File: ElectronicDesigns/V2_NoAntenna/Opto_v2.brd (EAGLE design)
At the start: 87.5 x 48 mm, 5 parts, among them U1 TLV1117-18IDCYG3

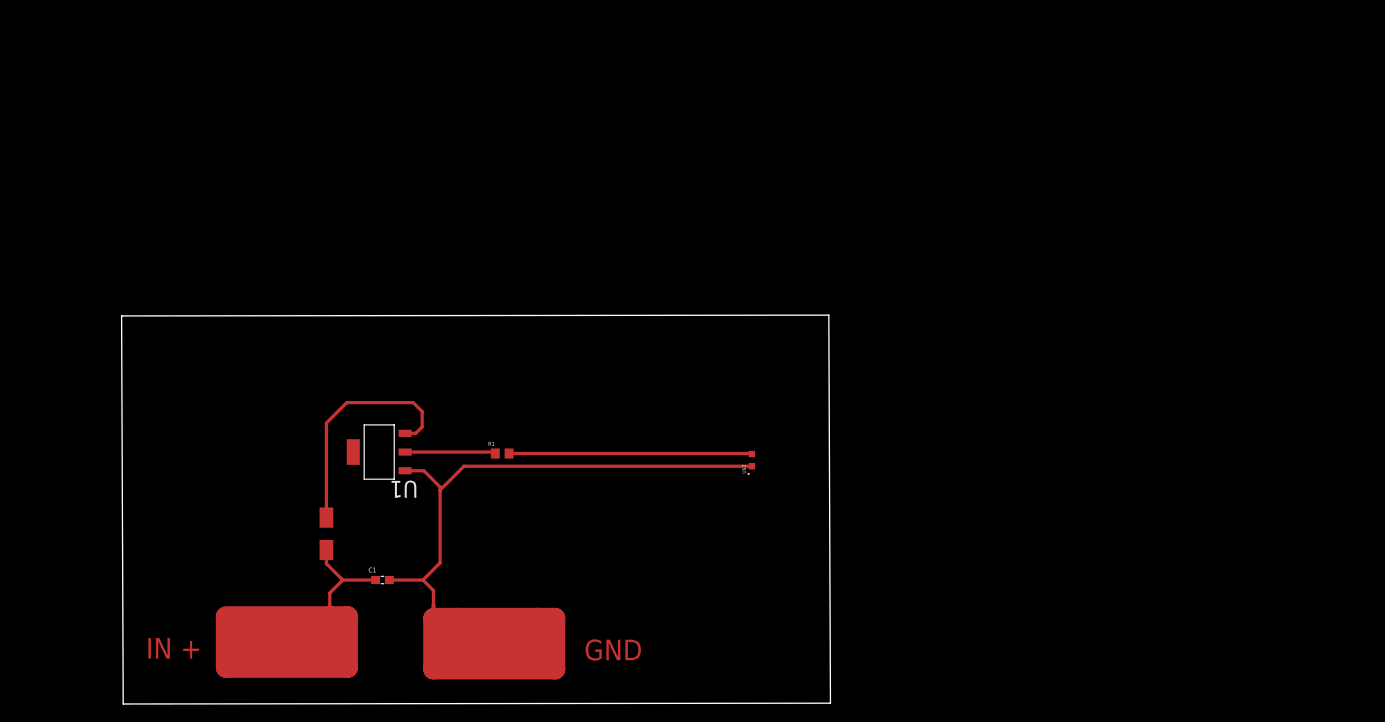
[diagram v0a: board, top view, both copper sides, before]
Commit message: antenna-circuit assembled
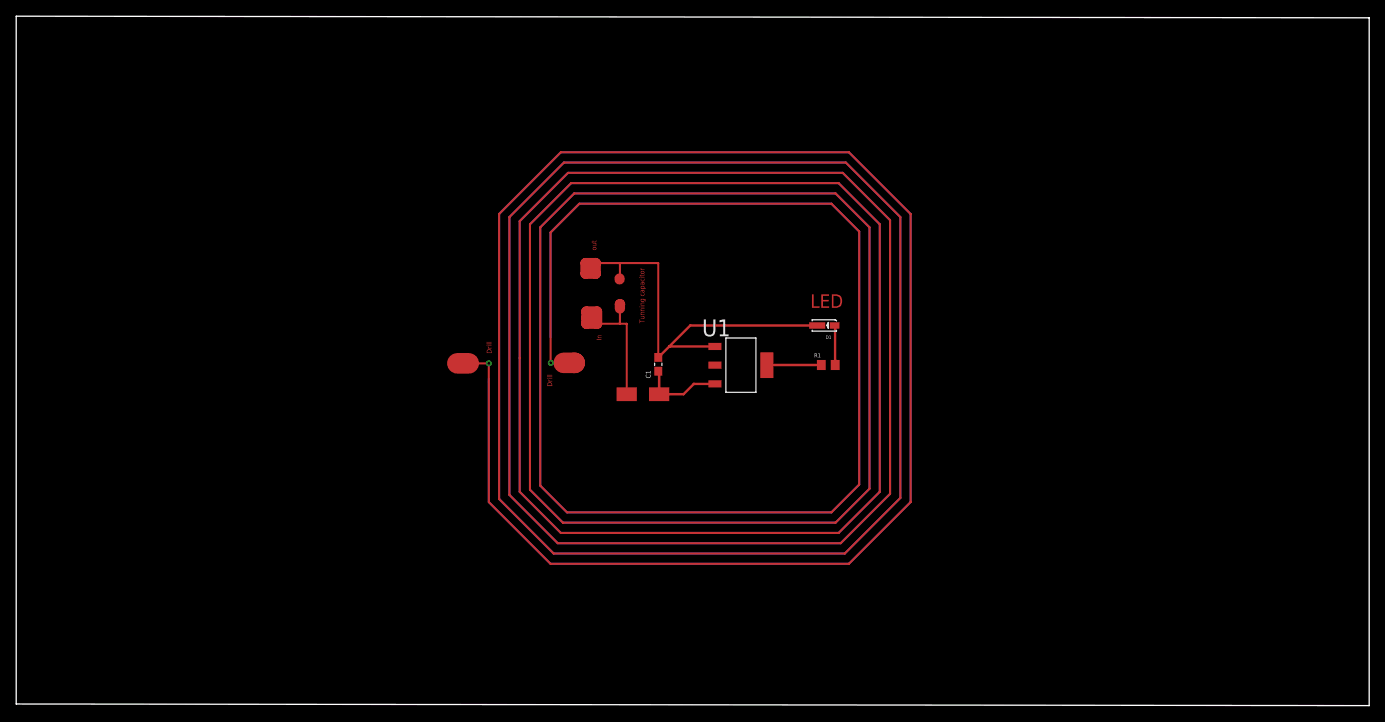
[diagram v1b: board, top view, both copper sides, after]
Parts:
- removed U$3: LED, LEDM1608X80:LEDM1608X80
- added D1: WL-SWTP3014, WL-SWTP:WL-SWTP_3014
- moved U1 45.9 mm to (73.4, 41.7), turned to 0 degrees
- moved C1 43.2 mm to (63.2, 41.8), turned to 90 degrees
- moved U$1 42.7 mm to (61.3, 38.1), turned to 0 degrees
- moved R1 41.7 mm to (84.2, 41.7)
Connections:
- net GND: now also D1.1; no longer U$3.C
- net IN+: no longer C1.1
- net N$1: now also U1.4; no longer U1.2
- net N$2: now also D1.2; no longer U$3.A
- net N$4: now also C1.1
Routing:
- net N$3: track 0.00 -> 538.5 mm, vias 0 -> 1
- net N$8: track 0.00 -> 532.7 mm
- net GND2: track 0.00 -> 465.6 mm, vias 0 -> 1
- net GND1: track 0.00 -> 459.3 mm
- net GND: track 148.3 -> 53.4 mm
- net IN+: track 95.6 -> 22.2 mm
- net N$2: track 30.0 -> 4.90 mm
- net N$4: track 29.3 -> 10.3 mm
- net N$1: track 11.2 -> 6.74 mm
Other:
- board size 87.5 x 48 mm -> 167 x 85.1 mm
- board text added: "Drill"
- board text added: "In"
- board text added: "LED"
- board text added: "Tunning capacitor"
- board text added: "out"
- board text removed: "GND"
- board text removed: "IN +"

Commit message: printings
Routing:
- net OUT: track 0.00 -> 1073.1 mm, vias 0 -> 1
- net IN: track 0.00 -> 928.0 mm, vias 0 -> 1
- net N$3: track 538.5 -> 0.00 mm, vias 1 -> 0
- net N$8: track 532.7 -> 0.00 mm
- net GND2: track 465.6 -> 0.00 mm, vias 1 -> 0
- net GND1: track 459.3 -> 0.00 mm
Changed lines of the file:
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@@
 <wire x1="85.075" y1="46.565" x2="85.015" y2="46.625" width="0.3048" layer="1"/>
 </signal>
-<signal name="N$8">
-<wire x1="42.329" y1="40.065" x2="42.329" y2="39.655" width="0.254" layer="16"/>
-<wire x1="42.329" y1="39.655" x2="42.329" y2="24.825" width="0.254" layer="16"/>
-<wire x1="49.949" y1="17.205" x2="42.329" y2="24.825" width="0.254" layer="16"/>
-<wire x1="49.949" y1="17.205" x2="86.779" y2="17.205" width="0.254" layer="16"/>
-<wire x1="86.779" y1="17.205" x2="94.399" y2="24.825" width="0.254" layer="16"/>
-<wire x1="94.399" y1="24.825" x2="94.399" y2="60.385" width="0.254" layer="16"/>
-<wire x1="94.399" y1="60.385" x2="86.779" y2="68.005" width="0.254" layer="16"/>
-<wire x1="86.779" y1="68.005" x2="51.219" y2="68.005" width="0.254" layer="16"/>
-<wire x1="51.219" y1="68.005" x2="43.599" y2="60.385" width="0.254" layer="16"/>
-<wire x1="43.599" y1="60.385" x2="43.599" y2="25.206" width="0.254" layer="16"/>
-<wire x1="43.599" y1="25.206" x2="50.33" y2="18.475" width="0.254" layer="16"/>
-<wire x1="50.33" y1="18.475" x2="86.271" y2="18.475" width="0.254" layer="16"/>
-<wire x1="86.271" y1="18.475" x2="93.129" y2="25.333" width="0.254" layer="16"/>
-<wire x1="93.129" y1="25.333" x2="93.129" y2="60.004" width="0.254" layer="16"/>
-<wire x1="93.129" y1="60.004" x2="86.398" y2="66.735" width="0.254" layer="16"/>
-<wire x1="86.398" y1="66.735" x2="51.6" y2="66.735" width="0.254" layer="16"/>
-<wire x1="51.6" y1="66.735" x2="44.869" y2="60.004" width="0.254" layer="16"/>
-<wire x1="44.869" y1="60.004" x2="44.869" y2="25.714" width="0.254" layer="16"/>
-<wire x1="44.869" y1="25.714" x2="50.838" y2="19.745" width="0.254" layer="16"/>
-<wire x1="50.838" y1="19.745" x2="85.763" y2="19.745" width="0.254" layer="16"/>
-<wire x1="85.763" y1="19.745" x2="91.859" y2="25.841" width="0.254" layer="16"/>
-<wire x1="91.859" y1="25.841" x2="91.859" y2="59.623" width="0.254" layer="16"/>
-<wire x1="91.859" y1="59.623" x2="86.017" y2="65.465" width="0.254" layer="16"/>
-<wire x1="86.017" y1="65.465" x2="52.108" y2="65.465" width="0.254" layer="16"/>
-<wire x1="52.108" y1="65.465" x2="46.139" y2="59.496" width="0.254" layer="16"/>
-<wire x1="46.139" y1="59.496" x2="46.139" y2="42.605" width="0.254" layer="16"/>
-</signal>
-<signal name="GND1">
-<wire x1="46.139" y1="26.095" x2="46.139" y2="42.605" width="0.254" layer="16"/>
-<wire x1="51.219" y1="21.015" x2="46.139" y2="26.095" width="0.254" layer="16"/>
-<wire x1="85.509" y1="21.015" x2="51.219" y2="21.015" width="0.254" layer="16"/>
-<wire x1="90.589" y1="26.095" x2="85.509" y2="21.015" width="0.254" layer="16"/>
-<wire x1="90.589" y1="59.115" x2="90.589" y2="26.095" width="0.254" layer="16"/>
-<wire x1="85.509" y1="64.195" x2="90.589" y2="59.115" width="0.254" layer="16"/>
-<wire x1="52.489" y1="64.195" x2="85.509" y2="64.195" width="0.254" layer="16"/>
-<wire x1="47.409" y1="59.115" x2="52.489" y2="64.195" width="0.254" layer="16"/>
-<wire x1="47.409" y1="26.349" x2="47.409" y2="59.115" width="0.254" layer="16"/>
-<wire x1="51.473" y1="22.285" x2="47.409" y2="26.349" width="0.254" layer="16"/>
-<wire x1="51.473" y1="22.285" x2="85.128" y2="22.285" width="0.254" layer="16"/>
-<wire x1="85.128" y1="22.285" x2="89.319" y2="26.476" width="0.254" layer="16"/>
-<wire x1="89.319" y1="26.476" x2="89.319" y2="58.734" width="0.254" layer="16"/>
-<wire x1="89.319" y1="58.734" x2="85.128" y2="62.925" width="0.254" layer="16"/>
-<wire x1="85.128" y1="62.925" x2="52.87" y2="62.925" width="0.254" layer="16"/>
-<wire x1="52.87" y1="62.925" x2="48.679" y2="58.734" width="0.254" layer="16"/>
-<wire x1="48.679" y1="58.734" x2="48.679" y2="26.857" width="0.254" layer="16"/>
-<wire x1="48.679" y1="26.857" x2="51.981" y2="23.555" width="0.254" layer="16"/>
-<wire x1="51.981" y1="23.555" x2="84.62" y2="23.555" width="0.254" layer="16"/>
-<wire x1="84.62" y1="23.555" x2="88.049" y2="26.984" width="0.254" layer="16"/>
-<wire x1="88.049" y1="26.984" x2="88.049" y2="58.226" width="0.254" layer="16"/>
-<wire x1="88.049" y1="58.226" x2="84.62" y2="61.655" width="0.254" layer="16"/>
-<wire x1="84.62" y1="61.655" x2="53.505" y2="61.655" width="0.254" layer="16"/>
-<wire x1="53.505" y1="61.655" x2="49.949" y2="58.099" width="0.254" layer="16"/>
-<wire x1="49.949" y1="58.099" x2="49.949" y2="45.145" width="0.254" layer="16"/>
-</signal>
-<signal name="N$3">
+<signal name="OUT">
 <wire x1="42.329" y1="24.825" x2="42.329" y2="41.95" width="0.254" layer="1"/>
 <wire x1="49.949" y1="17.205" x2="42.329" y2="24.825" width="0.254" layer="1"/>
@@
 <wire x1="39.85" y1="41.95" x2="38.445" y2="41.95" width="2.54" layer="1"/>
 <via x="42.329" y="41.95" extent="1-16" drill="0.35"/>
+<wire x1="42.329" y1="40.065" x2="42.329" y2="39.915" width="0.254" layer="16"/>
+<wire x1="42.329" y1="39.915" x2="42.329" y2="24.825" width="0.254" layer="16"/>
+<wire x1="49.949" y1="17.205" x2="42.329" y2="24.825" width="0.254" layer="16"/>
+<wire x1="49.949" y1="17.205" x2="86.779" y2="17.205" width="0.254" layer="16"/>
+<wire x1="86.779" y1="17.205" x2="94.399" y2="24.825" width="0.254" layer="16"/>
+<wire x1="94.399" y1="24.825" x2="94.399" y2="60.385" width="0.254" layer="16"/>
+<wire x1="94.399" y1="60.385" x2="86.779" y2="68.005" width="0.254" layer="16"/>
+<wire x1="86.779" y1="68.005" x2="51.219" y2="68.005" width="0.254" layer="16"/>
+<wire x1="51.219" y1="68.005" x2="43.599" y2="60.385" width="0.254" layer="16"/>
+<wire x1="43.599" y1="60.385" x2="43.599" y2="25.206" width="0.254" layer="16"/>
+<wire x1="43.599" y1="25.206" x2="50.33" y2="18.475" width="0.254" layer="16"/>
+<wire x1="50.33" y1="18.475" x2="86.271" y2="18.475" width="0.254" layer="16"/>
+<wire x1="86.271" y1="18.475" x2="93.129" y2="25.333" width="0.254" layer="16"/>
+<wire x1="93.129" y1="25.333" x2="93.129" y2="60.004" width="0.254" layer="16"/>
+<wire x1="93.129" y1="60.004" x2="86.398" y2="66.735" width="0.254" layer="16"/>
+<wire x1="86.398" y1="66.735" x2="51.6" y2="66.735" width="0.254" layer="16"/>
+<wire x1="51.6" y1="66.735" x2="44.869" y2="60.004" width="0.254" layer="16"/>
+<wire x1="44.869" y1="60.004" x2="44.869" y2="25.714" width="0.254" layer="16"/>
+<wire x1="44.869" y1="25.714" x2="50.838" y2="19.745" width="0.254" layer="16"/>
+<wire x1="50.838" y1="19.745" x2="85.763" y2="19.745" width="0.254" layer="16"/>
+<wire x1="85.763" y1="19.745" x2="91.859" y2="25.841" width="0.254" layer="16"/>
+<wire x1="91.859" y1="25.841" x2="91.859" y2="59.623" width="0.254" layer="16"/>
+<wire x1="91.859" y1="59.623" x2="86.017" y2="65.465" width="0.254" layer="16"/>
+<wire x1="86.017" y1="65.465" x2="52.108" y2="65.465" width="0.254" layer="16"/>
+<wire x1="52.108" y1="65.465" x2="46.139" y2="59.496" width="0.254" layer="16"/>
+<wire x1="46.139" y1="59.496" x2="46.139" y2="42.605" width="0.254" layer="16"/>
+<wire x1="42.329" y1="40.065" x2="42.329" y2="41.95" width="0.254" layer="16"/>
 </signal>
-<signal name="GND2">
+<signal name="IN">
 <wire x1="46.139" y1="26.095" x2="46.139" y2="42.605" width="0.254" layer="1"/>
 <wire x1="51.219" y1="21.015" x2="46.139" y2="26.095" width="0.254" layer="1"/>
@@
 <wire x1="49.949" y1="58.099" x2="49.949" y2="42.01" width="0.254" layer="1"/>
 <wire x1="49.949" y1="42.01" x2="49.974" y2="42.01" width="0.254" layer="1"/>
+<wire x1="46.139" y1="26.095" x2="46.139" y2="42.605" width="0.254" layer="16"/>
+<wire x1="51.219" y1="21.015" x2="46.139" y2="26.095" width="0.254" layer="16"/>
+<wire x1="85.509" y1="21.015" x2="51.219" y2="21.015" width="0.254" layer="16"/>
+<wire x1="90.589" y1="26.095" x2="85.509" y2="21.015" width="0.254" layer="16"/>
+<wire x1="90.589" y1="59.115" x2="90.589" y2="26.095" width="0.254" layer="16"/>
+<wire x1="85.509" y1="64.195" x2="90.589" y2="59.115" width="0.254" layer="16"/>
+<wire x1="52.489" y1="64.195" x2="85.509" y2="64.195" width="0.254" layer="16"/>
+<wire x1="47.409" y1="59.115" x2="52.489" y2="64.195" width="0.254" layer="16"/>
+<wire x1="47.409" y1="26.349" x2="47.409" y2="59.115" width="0.254" layer="16"/>
+<wire x1="51.473" y1="22.285" x2="47.409" y2="26.349" width="0.254" layer="16"/>
+<wire x1="51.473" y1="22.285" x2="85.128" y2="22.285" width="0.254" layer="16"/>
+<wire x1="85.128" y1="22.285" x2="89.319" y2="26.476" width="0.254" layer="16"/>
+<wire x1="89.319" y1="26.476" x2="89.319" y2="58.734" width="0.254" layer="16"/>
+<wire x1="89.319" y1="58.734" x2="85.128" y2="62.925" width="0.254" layer="16"/>
+<wire x1="85.128" y1="62.925" x2="52.87" y2="62.925" width="0.254" layer="16"/>
+<wire x1="52.87" y1="62.925" x2="48.679" y2="58.734" width="0.254" layer="16"/>
+<wire x1="48.679" y1="58.734" x2="48.679" y2="26.857" width="0.254" layer="16"/>
+<wire x1="48.679" y1="26.857" x2="51.981" y2="23.555" width="0.254" layer="16"/>
+<wire x1="51.981" y1="23.555" x2="84.62" y2="23.555" width="0.254" layer="16"/>
+<wire x1="84.62" y1="23.555" x2="88.049" y2="26.984" width="0.254" layer="16"/>
+<wire x1="88.049" y1="26.984" x2="88.049" y2="58.226" width="0.254" layer="16"/>
+<wire x1="88.049" y1="58.226" x2="84.62" y2="61.655" width="0.254" layer="16"/>
+<wire x1="84.62" y1="61.655" x2="53.505" y2="61.655" width="0.254" layer="16"/>
+<wire x1="53.505" y1="61.655" x2="49.949" y2="58.099" width="0.254" layer="16"/>
+<wire x1="49.949" y1="58.099" x2="49.949" y2="45.365" width="0.254" layer="16"/>
+<wire x1="49.949" y1="45.365" x2="49.949" y2="45.145" width="0.254" layer="16"/>
+<wire x1="49.949" y1="45.145" x2="49.949" y2="42.035" width="0.254" layer="16"/>
+<wire x1="49.949" y1="42.035" x2="49.974" y2="42.01" width="0.254" layer="16"/>
 </signal>
 </signals>
